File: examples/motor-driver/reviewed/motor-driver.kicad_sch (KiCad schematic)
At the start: 19 parts, among them J1 VM 2.7-10.8V, J2 MOTOR A, J3 MOTOR B, J4 LOGIC, U1 DRV8833PW

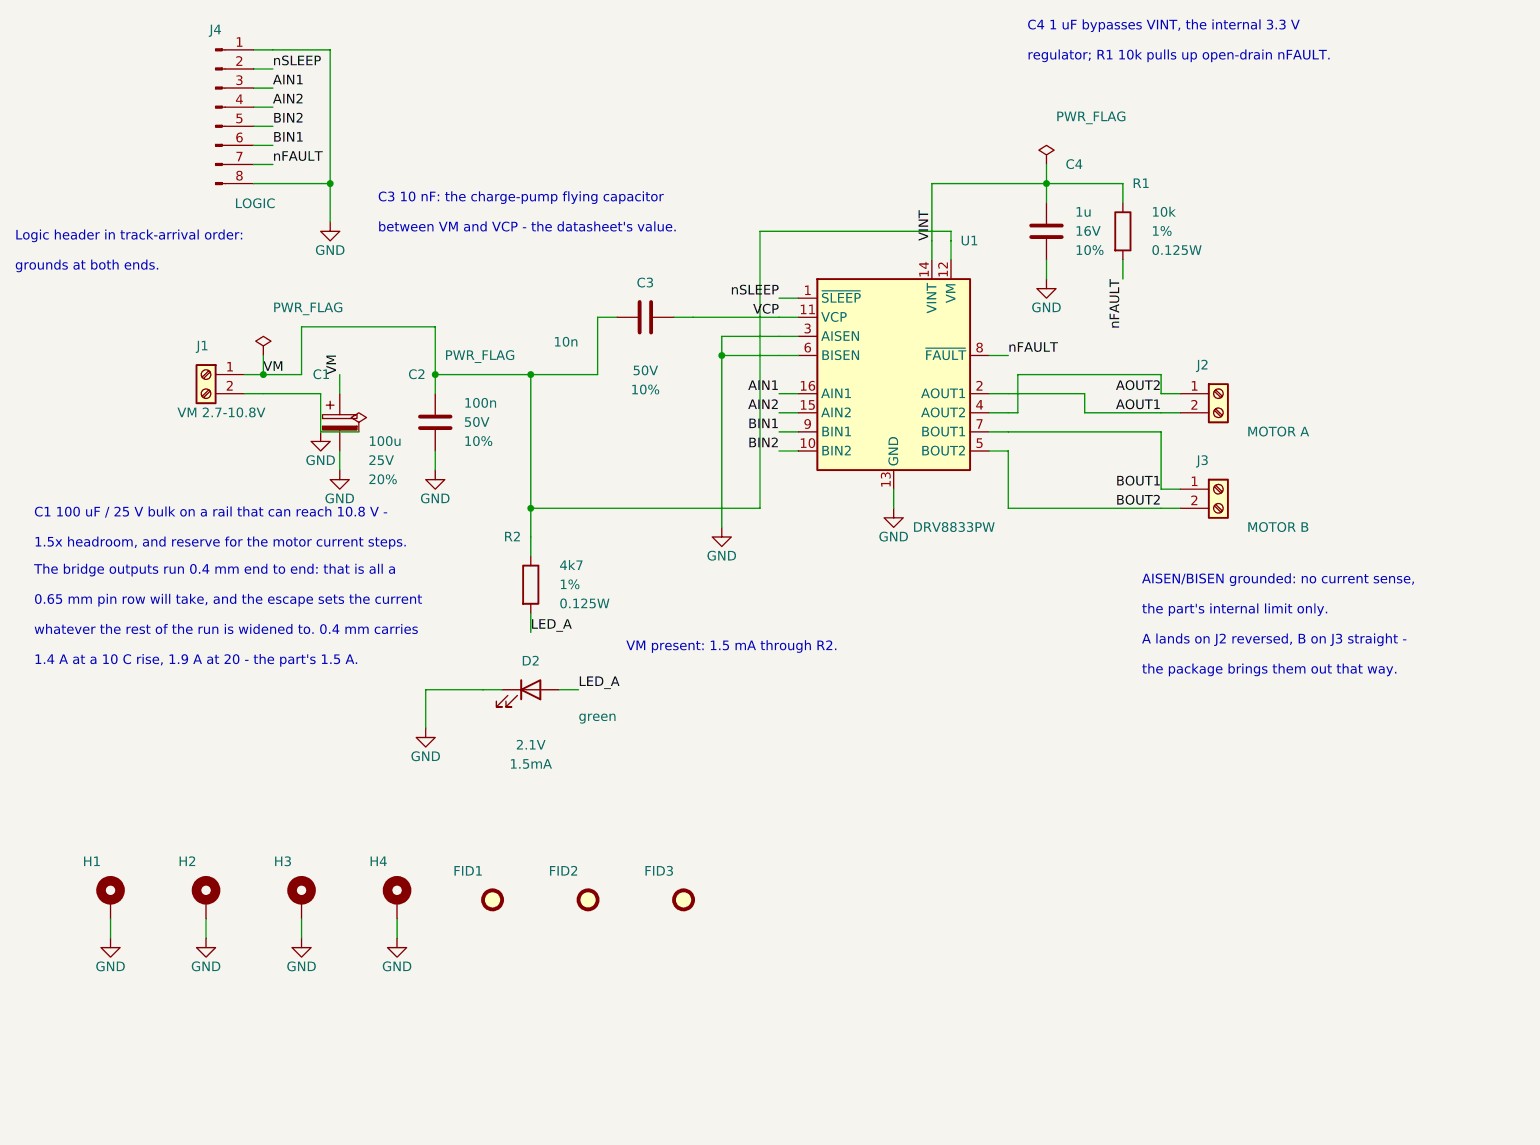
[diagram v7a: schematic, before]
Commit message: feat(examples): round twenty - fuse and clamp every input, state the ESR, damp the clock, control the mute
Redesign of the five worked examples for the items REVIEW.md left open:

- every power input gets a fuse in series and a TVS across the fused rail
  (a resettable fuse on the Pico carrier, whose Schottky already blocks a
  reversed supply); each sheet states what the clamp does not do
- the buck's output capacitor states the ESR the LM2596 loop is designed
  around (SNVS124G 9.1.3), derived from the ripple already on the sheet
- the FPGA's 12 MHz clock leaves its oscillator through 33 ohms
- the DAC's XSMT is driven from the FPGA with a pull-down instead of
  strapped high, so it comes up muted
- the op-amp filter's output goes through a 100 ohm isolation resistor

Generator fixes the round found: _surfaced pruned a via that tapped the
middle of a back-layer spine, and _chamfer_tracks cut the copper out from
under a via sitting a fraction along a leg; both left a net in two pieces
that KiCad's DRC reported. Pin stubs closer than 7.62 mm draw over each
other, so the new parts are spaced for it and the comments say why.

tools/example_images.py renders the README pictures from the regenerated
projects. All five reviewed variants pass their gates and KiCad's DRC on
both matrix versions; the as-generated variants each carry one more
blocking finding (spec.missing_esr). REVIEW.md 25 records the round.

Co-Authored-By: Claude Fable 5.1 <noreply@anthropic.com>
Claude-Session: https://claude.ai/code/session_017JKofiLFxXjzRRnBmFyXuQ
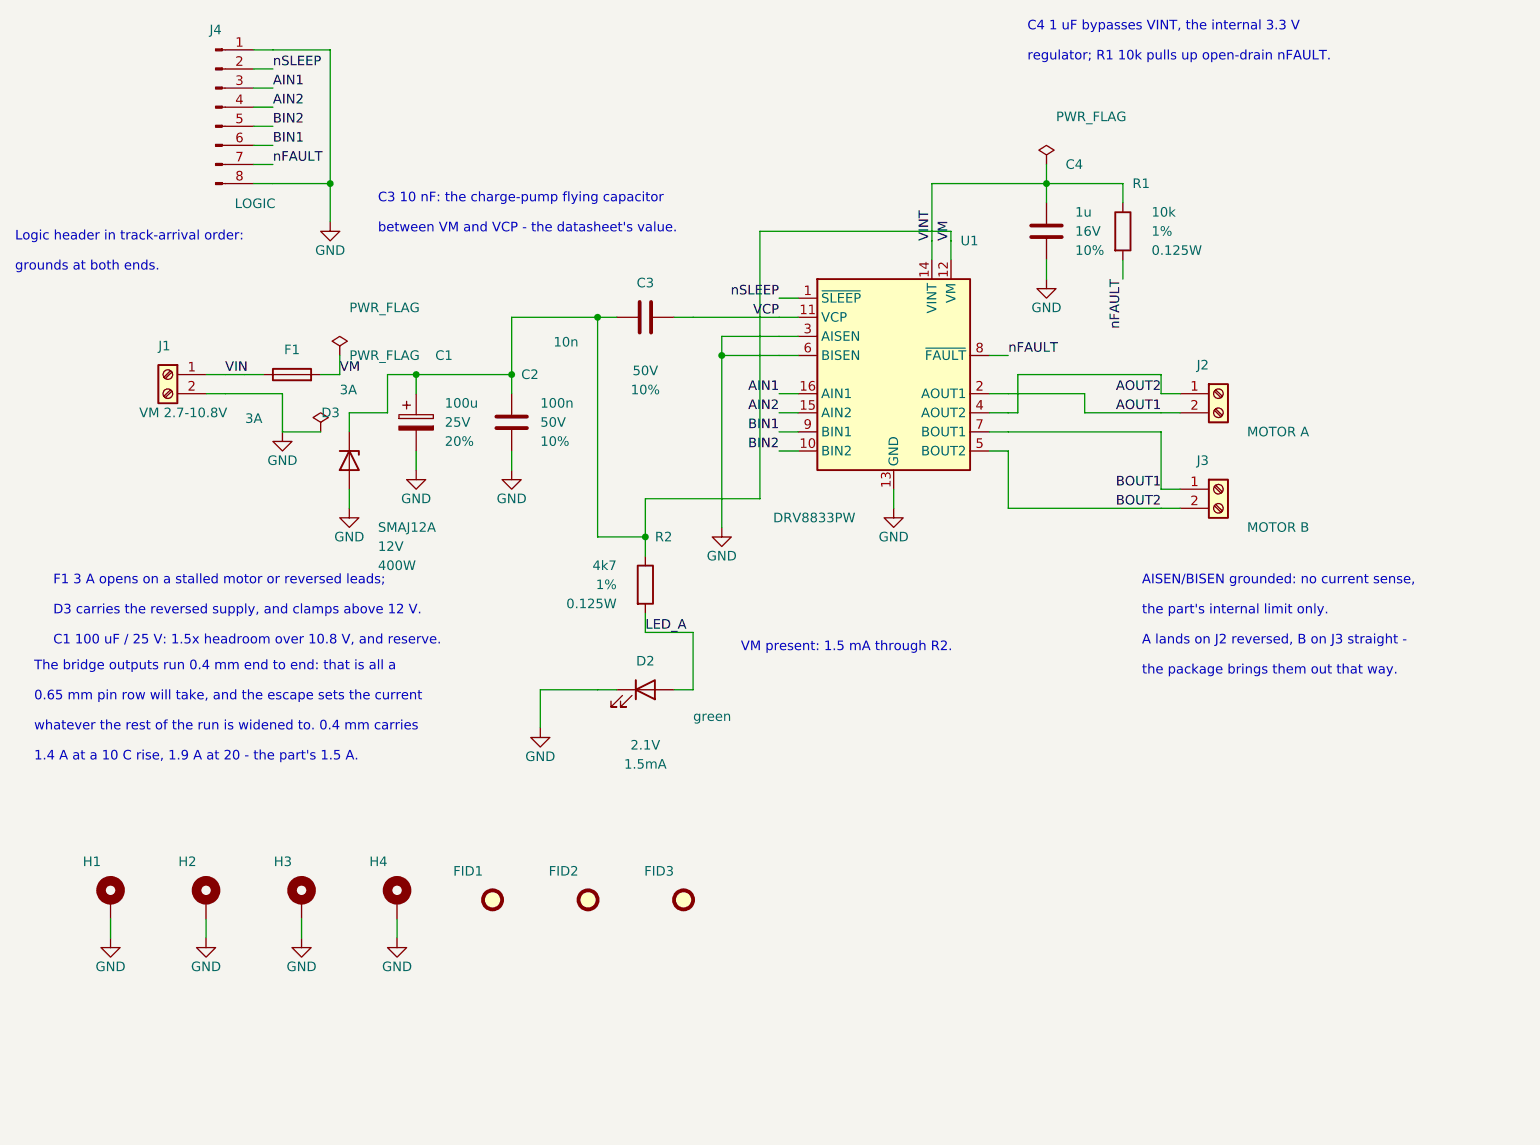
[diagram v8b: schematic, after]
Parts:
- added D3: SMAJ12A, Diode_SMD:D_SMA, symbol Device:D_Zener
- added F1: 3A, Fuse:Fuse_1206_3216Metric, symbol Device:Fuse
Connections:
- net GND: now also D3.2 (A)
- net VM: now also D3.1 (K), F1.2; no longer J1.1 (Pin_1)
- new net VIN: F1.1, J1.1 (Pin_1)
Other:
- note added: "C1 100 uF / 25 V: 1.5x headroom over 10.8 V, and reserve."
- note added: "D3 carries the reversed supply, and clamps above 12 V."
- note added: "F1 3 A opens on a stalled motor or reversed leads;"
- note removed: "1.5x headroom, and reserve for the motor current steps."
- note removed: "C1 100 uF / 25 V bulk on a rail that can reach 10.8 V -"
- moved on the sheet: C1, C2, D2, J1, R2
